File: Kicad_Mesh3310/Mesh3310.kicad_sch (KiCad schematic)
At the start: 12 parts, among them J1 USB device, SW2 "OK"

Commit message: Adding testpoints
Test pint on usb and SWD debug
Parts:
- added TP10: GND, TestPoint:TestPoint_Pad_D1.5mm, symbol Connector:TestPoint
- added TP11: USB_D-, TestPoint:TestPoint_Pad_D1.5mm, symbol Connector:TestPoint
- added TP12: USB_D+, TestPoint:TestPoint_Pad_D1.5mm, symbol Connector:TestPoint
- added TP9: VBUS, TestPoint:TestPoint_Pad_D1.5mm, symbol Connector:TestPoint
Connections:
- net GND: now also TP10.1
- net VBUS: now also TP9.1

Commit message: component placing
component placing
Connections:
- net USB_D+: now also TP12.1
- net USB_D-: now also TP11.1
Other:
- moved on the sheet: TP11, TP12
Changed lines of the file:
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@@
 	)
 	(junction
+		(at 237.49 96.52)
+		(diameter 0)
+		(color 0 0 0 0)
+	)
+	(junction
 		(at 234.95 82.55)
 		(diameter 0)
@@
 	)
 	(junction
+		(at 234.95 91.44)
+		(diameter 0)
+		(color 0 0 0 0)
+	)
+	(junction
 		(at 243.84 91.44)
 		(diameter 0)
@@
 	(wire
 		(pts
+			(xy 237.49 99.06) (xy 237.49 96.52)
+		)
+		(stroke
+			(width 0)
+			(type default)
+		)
+	)
+	(wire
+		(pts
 			(xy 110.49 45.72) (xy 135.89 45.72)
 		)
@@
 	(wire
 		(pts
-			(xy 243.84 96.52) (xy 232.41 96.52)
+			(xy 243.84 96.52) (xy 237.49 96.52)
 		)
 		(stroke
@@
 	(wire
 		(pts
-			(xy 243.84 91.44) (xy 232.41 91.44)
+			(xy 243.84 91.44) (xy 234.95 91.44)
 		)
 		(stroke
@@
 	(wire
 		(pts
+			(xy 234.95 99.06) (xy 234.95 91.44)
+		)
+		(stroke
+			(width 0)
+			(type default)
+		)
+	)
+	(wire
+		(pts
 			(xy 82.55 93.98) (xy 62.23 93.98)
 		)
@@
 		)
 	)
+	(wire
+		(pts
+			(xy 237.49 96.52) (xy 232.41 96.52)
+		)
+		(stroke
+			(width 0)
+			(type default)
+		)
+	)
+	(wire
+		(pts
+			(xy 234.95 91.44) (xy 232.41 91.44)
+		)
+		(stroke
+			(width 0)
+			(type default)
+		)
+	)
 	(bus
 		(pts
@@
 	(symbol
 		(lib_id "Connector:TestPoint")
-		(at 229.87 88.9 90)
+		(at 234.95 99.06 180)
 		(unit 1)
 		(exclude_from_sim no)
@@
 		(dnp no)
 		(property "Reference" "TP11"
-			(at 227.33 87.122 90)
+			(at 233.172 101.6 90)
 			(effects
 				(font
@@
 		)
 		(property "Value" "USB_D-"
-			(at 225.806 85.09 90)
+			(at 231.14 101.6 90)
 			(effects
 				(font
@@
 		)
 		(property "Footprint" "TestPoint:TestPoint_Pad_D1.5mm"
-			(at 229.87 83.82 0)
+			(at 229.87 99.06 0)
 			(effects
 				(font
@@
 		)
 		(property "Datasheet" "~"
-			(at 229.87 83.82 0)
+			(at 229.87 99.06 0)
 			(effects
 				(font
@@
 		)
 		(property "Description" "test point"
-			(at 229.87 88.9 0)
+			(at 234.95 99.06 0)
 			(effects
 				(font
@@
 	(symbol
 		(lib_id "Connector:TestPoint")
-		(at 229.87 93.98 90)
+		(at 237.49 99.06 180)
 		(unit 1)
 		(exclude_from_sim no)
@@
 		(dnp no)
 		(property "Reference" "TP12"
-			(at 228.092 95.758 90)
+			(at 239.268 100.838 90)
 			(effects
 				(font
@@
 		)
 		(property "Value" "USB_D+"
-			(at 227.076 97.536 90)
+			(at 241.046 101.854 90)
 			(effects
 				(font
@@
 		)
 		(property "Footprint" "TestPoint:TestPoint_Pad_D1.5mm"
-			(at 229.87 88.9 0)
+			(at 232.41 99.06 0)
 			(effects
 				(font
@@
 		)
 		(property "Datasheet" "~"
-			(at 229.87 88.9 0)
+			(at 232.41 99.06 0)
 			(effects
 				(font
@@
 		)
 		(property "Description" "test point"
-			(at 229.87 93.98 0)
+			(at 237.49 99.06 0)
 			(effects
 				(font

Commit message: Cleaning and placing
Cleaning and placing components
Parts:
- H1, H2, H3, H4, H5, H6, H7: footprint Parts:2mm_mounting_hole_sig -> mesh3310_footprints:2mm_mounting_hole_sig
- J1: footprint mesh3310:USB_C_Receptacle_HRO_TYPE-C-31-M-12 -> mesh3310_footprints:USB_C_Receptacle_HRO_TYPE-C-31-M-12
- SW2: footprint Parts:3310_key -> mesh3310_footprints:3310_key
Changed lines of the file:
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@@
 			)
 		)
-		(property "Footprint" "Parts:2mm_mounting_hole_sig"
+		(property "Footprint" "mesh3310_footprints:2mm_mounting_hole_sig"
 			(at 107.95 175.26 0)
 			(effects
@@
 			)
 		)
-		(property "Footprint" "Parts:2mm_mounting_hole_sig"
+		(property "Footprint" "mesh3310_footprints:2mm_mounting_hole_sig"
 			(at 100.33 175.26 0)
 			(effects
@@
 			)
 		)
-		(property "Footprint" "Parts:2mm_mounting_hole_sig"
+		(property "Footprint" "mesh3310_footprints:2mm_mounting_hole_sig"
 			(at 146.05 175.26 0)
 			(effects
@@
 			)
 		)
-		(property "Footprint" "Parts:2mm_mounting_hole_sig"
+		(property "Footprint" "mesh3310_footprints:2mm_mounting_hole_sig"
 			(at 115.57 175.26 0)
 			(effects
@@
 			)
 		)
-		(property "Footprint" "Parts:2mm_mounting_hole_sig"
+		(property "Footprint" "mesh3310_footprints:2mm_mounting_hole_sig"
 			(at 130.81 175.26 0)
 			(effects
@@
 			)
 		)
-		(property "Footprint" "Parts:2mm_mounting_hole_sig"
+		(property "Footprint" "mesh3310_footprints:2mm_mounting_hole_sig"
 			(at 138.43 175.26 0)
 			(effects
@@
 			)
 		)
-		(property "Footprint" "Parts:2mm_mounting_hole_sig"
+		(property "Footprint" "mesh3310_footprints:2mm_mounting_hole_sig"
 			(at 123.19 175.26 0)
 			(effects
@@
 			)
 		)
-		(property "Footprint" "mesh3310:USB_C_Receptacle_HRO_TYPE-C-31-M-12"
+		(property "Footprint" "mesh3310_footprints:USB_C_Receptacle_HRO_TYPE-C-31-M-12"
 			(at 256.54 92.71 0)
 			(effects
@@
 			)
 		)
-		(property "Footprint" "Parts:3310_key"
+		(property "Footprint" "mesh3310_footprints:3310_key"
 			(at 109.22 33.02 0)
 			(effects

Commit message: RF designing
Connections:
- no-connect marks 9 -> 11
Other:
- removed sheet NFC
- note added: "Used with permission / community credit Reference designs and libs from badge.team MCU sections adapted from CyberAegg."
- note removed: "Used with permission / community credit Reference designs and libs from badge.team MCU and RF sections adapted from CyberAegg."
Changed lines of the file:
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@@
 		)
 	)
-	(text "Used with permission / community credit\nReference designs and libs from badge.team\nMCU and RF sections adapted from CyberAegg.\n\n"
+	(text "Used with permission / community credit\nReference designs and libs from badge.team\nMCU sections adapted from CyberAegg.\n\n"
 		(exclude_from_sim no)
 		(at 240.03 176.53 0)
@@
 	)
 	(no_connect
+		(at 135.89 43.18)
+	)
+	(no_connect
 		(at 179.07 29.21)
 	)
@@
 	)
 	(no_connect
+		(at 135.89 45.72)
+	)
+	(no_connect
 		(at 245.11 105.41)
 	)
@@
 	(wire
 		(pts
-			(xy 110.49 43.18) (xy 135.89 43.18)
-		)
-		(stroke
-			(width 0)
-			(type default)
-		)
-	)
-	(wire
-		(pts
 			(xy 195.58 130.81) (xy 175.26 130.81)
 		)
@@
 	(wire
 		(pts
-			(xy 110.49 45.72) (xy 135.89 45.72)
-		)
-		(stroke
-			(width 0)
-			(type default)
-		)
-	)
-	(wire
-		(pts
 			(xy 200.66 31.75) (xy 179.07 31.75)
 		)
@@
 	)
 	(sheet
-		(at 82.55 41.91)
-		(size 27.94 5.08)
-		(exclude_from_sim no)
-		(in_bom yes)
-		(on_board yes)
-		(dnp no)
-		(stroke
-			(width 0.1524)
-			(type solid)
-		)
-		(fill
-			(color 0 0 0 0.0000)
-		)
-		(property "Sheetname" "NFC"
-			(at 82.296 41.148 0)
-			(effects
-				(font
-					(size 1.27 1.27)
-				)
-				(justify left bottom)
-			)
-		)
-		(property "Sheetfile" "nfc.kicad_sch"
-			(at 82.55 47.5746 0)
-			(effects
-				(font
-					(size 1.27 1.27)
-				)
-				(justify left top)
-			)
-		)
-		(pin "NFC1" input
-			(at 110.49 43.18 0)
-			(effects
-				(font
-					(size 1.27 1.27)
-				)
-				(justify right)
-			)
-		)
-		(pin "NFC2" input
-			(at 110.49 45.72 0)
-			(effects
-				(font
-					(size 1.27 1.27)
-				)
-				(justify right)
-			)
-		)
-		(instances
-			(project "Mesh3310"
-				(path "/8d65c5ef-7a02-4454-aee5-ab9c49e4aeab"
-					(page "5")
-				)
-			)
-		)
-	)
-	(sheet
 		(at 41.91 67.31)
 		(size 20.32 40.64)
@@
 			(project "Mesh3310"
 				(path "/8d65c5ef-7a02-4454-aee5-ab9c49e4aeab"
-					(page "7")
+					(page "6")
 				)
 			)
@@
 			(project "Mesh3310"
 				(path "/8d65c5ef-7a02-4454-aee5-ab9c49e4aeab"
-					(page "6")
+					(page "5")
 				)
 			)

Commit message: cleanup
schematic cleanup
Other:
- removed sheet QWIIC
- sheet INTERFACES ports: added SCL, SDA; removed none
- note added: "JLC04161H-7628 Stackup Impendance calculator: https://jlcpcb.com/pcb-impedance-calculator"
- note added: "Used with permission / community credit Reference designs MCU sections adapted from CyberAegg. badge.team"
- note removed: "JLCPCB Inpedance control Stackup used: JLC04161H-7628 Stackup Impendance calculator: https://jlcpcb.com/pcb-impedance-calculator"
- note removed: "Used with permission / community credit Reference designs and libs from badge.team MCU sections adapted from CyberAegg."
- moved on the sheet: H1, H2, H3, H4, H5, H6, H7, J1, R1, R2, R8, SW2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

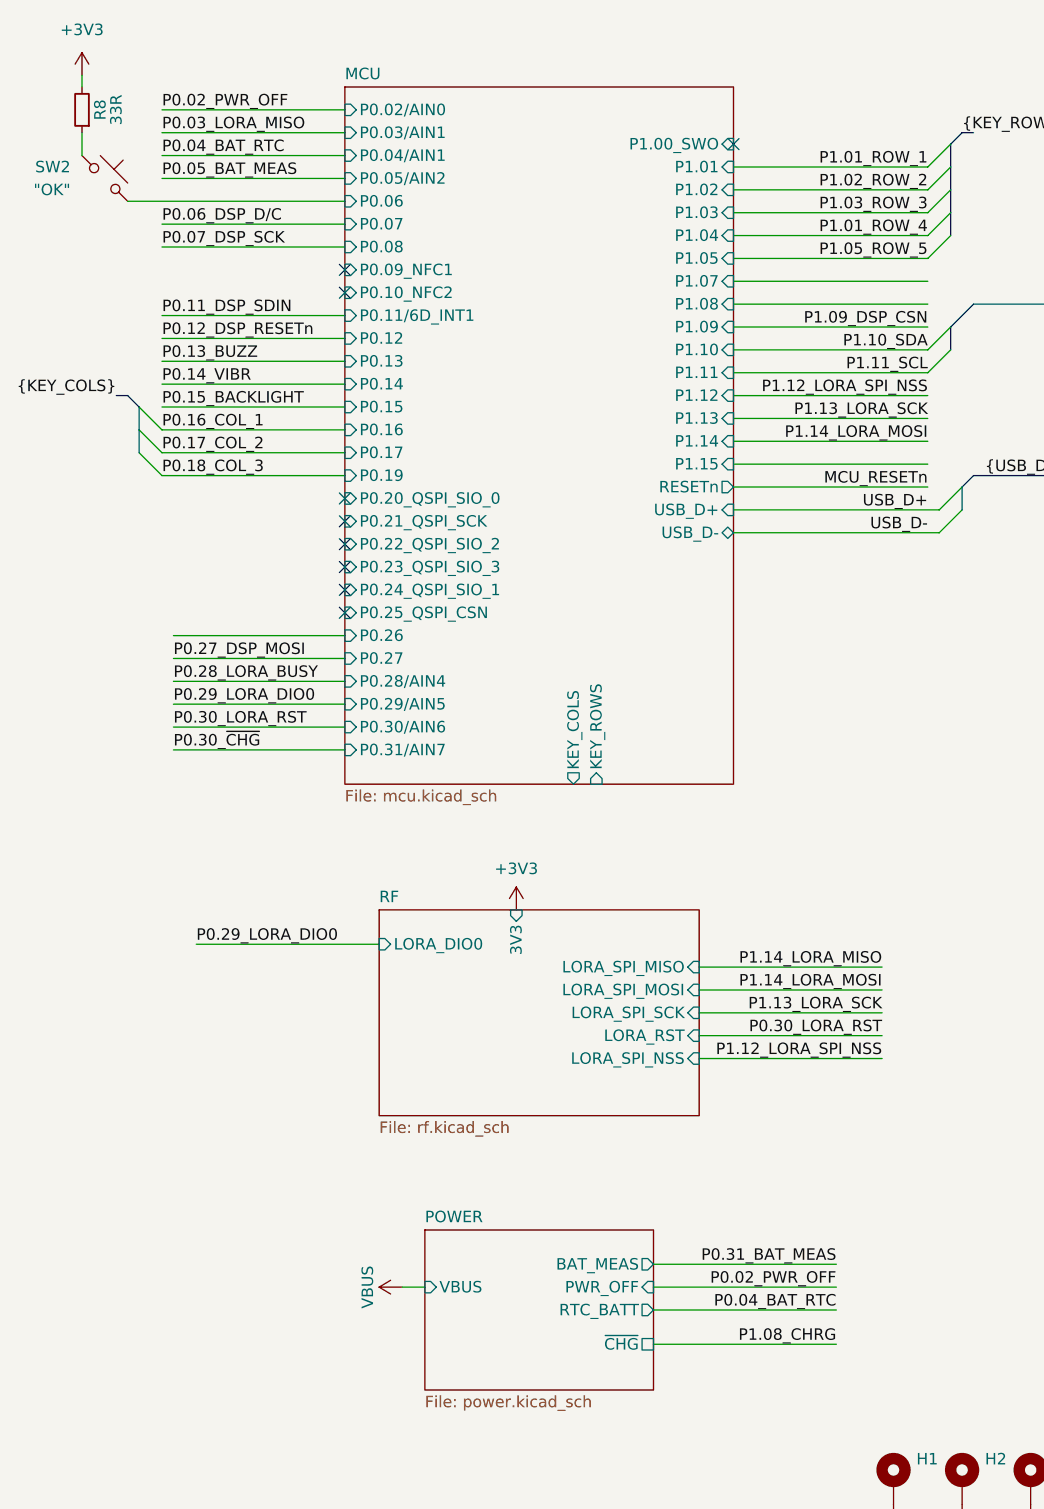
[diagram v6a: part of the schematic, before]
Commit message: Lora changes
Schematic changes to from RA to SOC
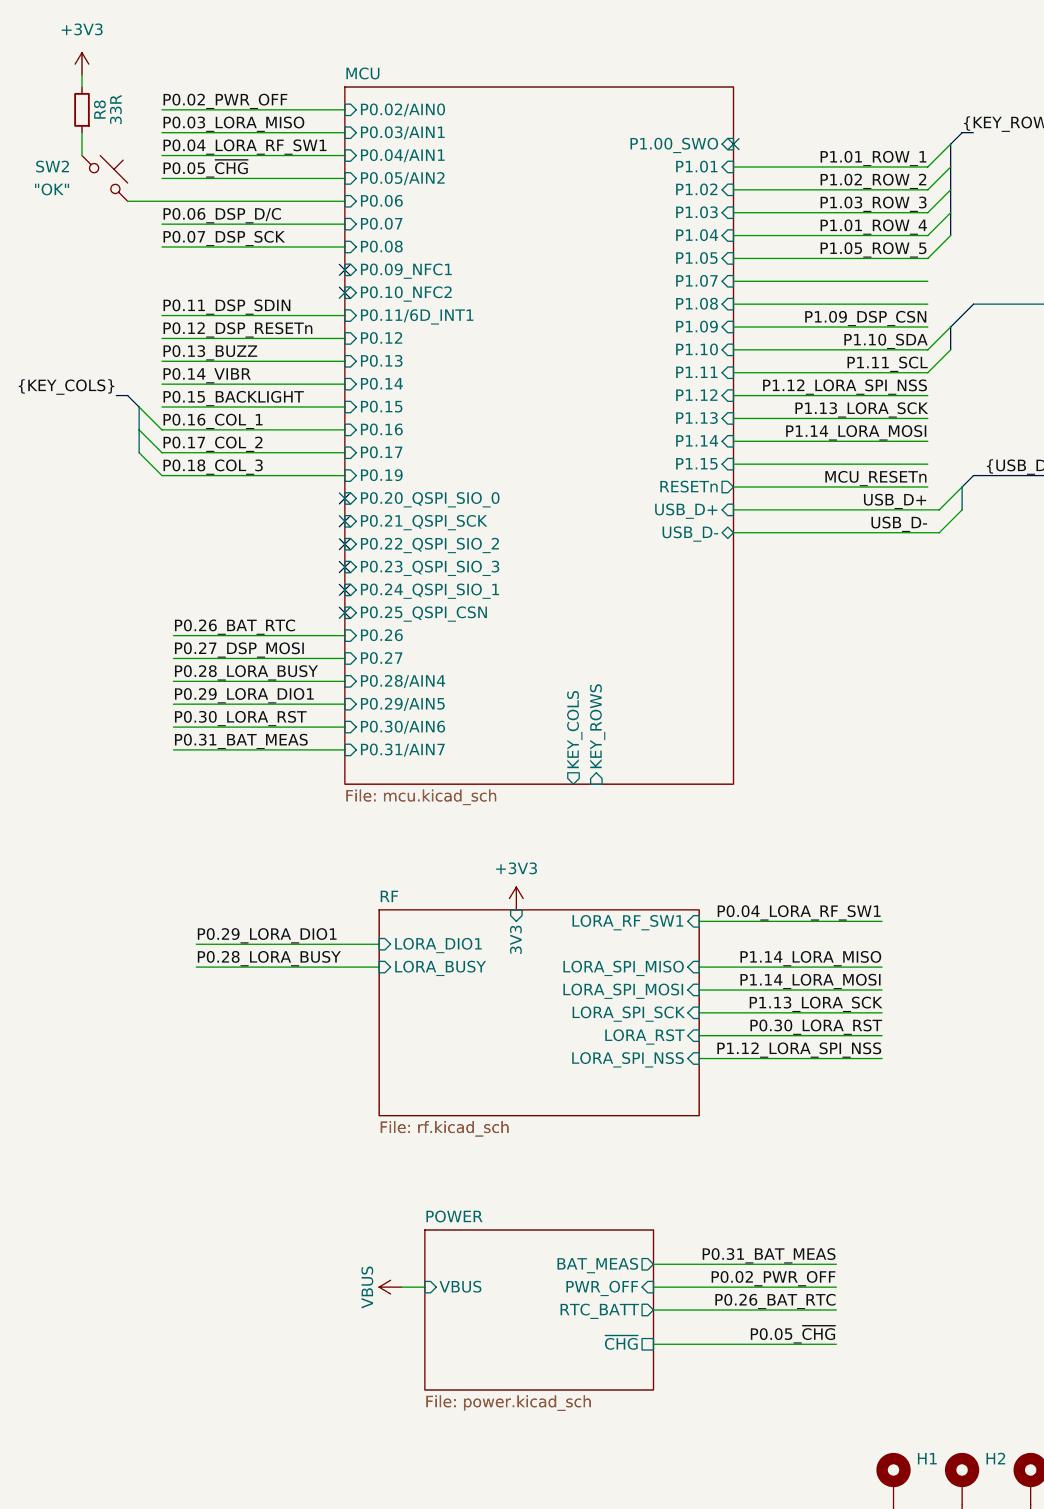
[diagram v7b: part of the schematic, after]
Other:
- sheet RF ports: added LORA_BUSY, LORA_DIO1, LORA_RF_SW1; removed LORA_DIO0
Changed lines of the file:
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@@
 		)
 	)
+	(wire
+		(pts
+			(xy 64.77 130.81) (xy 44.45 130.81)
+		)
+		(stroke
+			(width 0)
+			(type default)
+		)
+	)
 	(bus
 		(pts
@@
 	(wire
 		(pts
+			(xy 100.33 125.73) (xy 120.65 125.73)
+		)
+		(stroke
+			(width 0)
+			(type default)
+		)
+	)
+	(wire
+		(pts
 			(xy 100.33 140.97) (xy 120.65 140.97)
 		)
@@
 		)
 	)
-	(label "P1.08_CHRG"
+	(label "P0.05_~{CHG}"
 		(at 115.57 172.72 180)
 		(effects
@@
 		)
 	)
-	(label "P0.29_LORA_DIO0"
+	(label "P0.29_LORA_DIO1"
 		(at 44.45 128.27 0)
 		(effects
@@
 		)
 	)
+	(label "P0.04_LORA_RF_SW1"
+		(at 120.65 125.73 180)
+		(effects
+			(font
+				(size 1.27 1.27)
+			)
+			(justify right bottom)
+		)
+	)
 	(label "CC2"
 		(at 170.18 95.25 180)
@@
 		)
 	)
-	(label "P0.30_~{CHG}"
-		(at 41.91 106.68 0)
+	(label "P0.05_~{CHG}"
+		(at 40.64 43.18 0)
 		(effects
 			(font
@@
 		)
 	)
-	(label "P0.04_BAT_RTC"
-		(at 40.64 40.64 0)
+	(label "P0.26_BAT_RTC"
+		(at 41.91 93.98 0)
 		(effects
 			(font
@@
 		)
 	)
-	(label "P0.29_LORA_DIO0"
+	(label "P0.29_LORA_DIO1"
 		(at 41.91 101.6 0)
 		(effects
@@
 		)
 	)
+	(label "P0.04_LORA_RF_SW1"
+		(at 40.64 40.64 0)
+		(effects
+			(font
+				(size 1.27 1.27)
+			)
+			(justify left bottom)
+		)
+	)
 	(label "P1.14_LORA_MOSI"
 		(at 120.65 133.35 180)
@@
 		)
 	)
-	(label "P0.04_BAT_RTC"
+	(label "P0.26_BAT_RTC"
 		(at 115.57 168.91 180)
 		(effects
@@
 		)
 	)
+	(label "P0.28_LORA_BUSY"
+		(at 44.45 130.81 0)
+		(effects
+			(font
+				(size 1.27 1.27)
+			)
+			(justify left bottom)
+		)
+	)
 	(label "P1.12_LORA_SPI_NSS"
 		(at 120.65 140.97 180)
@@
 		)
 	)
-	(label "P0.05_BAT_MEAS"
-		(at 40.64 43.18 0)
+	(label "P0.31_BAT_MEAS"
+		(at 41.91 106.68 0)
 		(effects
 			(font
@@
 			)
 		)
-		(pin "LORA_DIO0" input
+		(pin "LORA_BUSY" input
+			(at 64.77 130.81 180)
+			(effects
+				(font
+					(size 1.27 1.27)
+				)
+				(justify left)
+			)
+		)
+		(pin "LORA_DIO1" input
 			(at 64.77 128.27 180)
 			(effects
@@
 			)
 		)
+		(pin "LORA_RF_SW1" input
+			(at 100.33 125.73 0)
+			(effects
+				(font
+					(size 1.27 1.27)
+				)
+				(justify right)
+			)
+		)

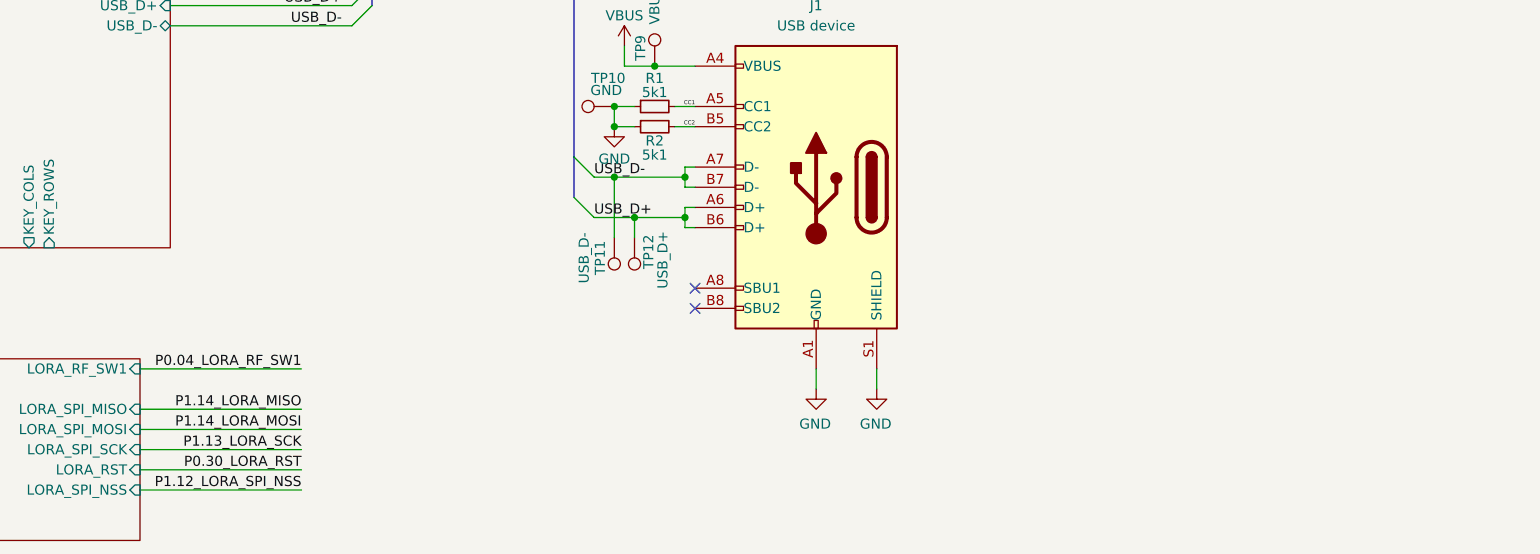
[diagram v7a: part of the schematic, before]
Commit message: Lora antenna replacement
Lora antenna replacement, added Nordic nRF 9151 for GPS , VoIP ,VoLTE-m , SIP
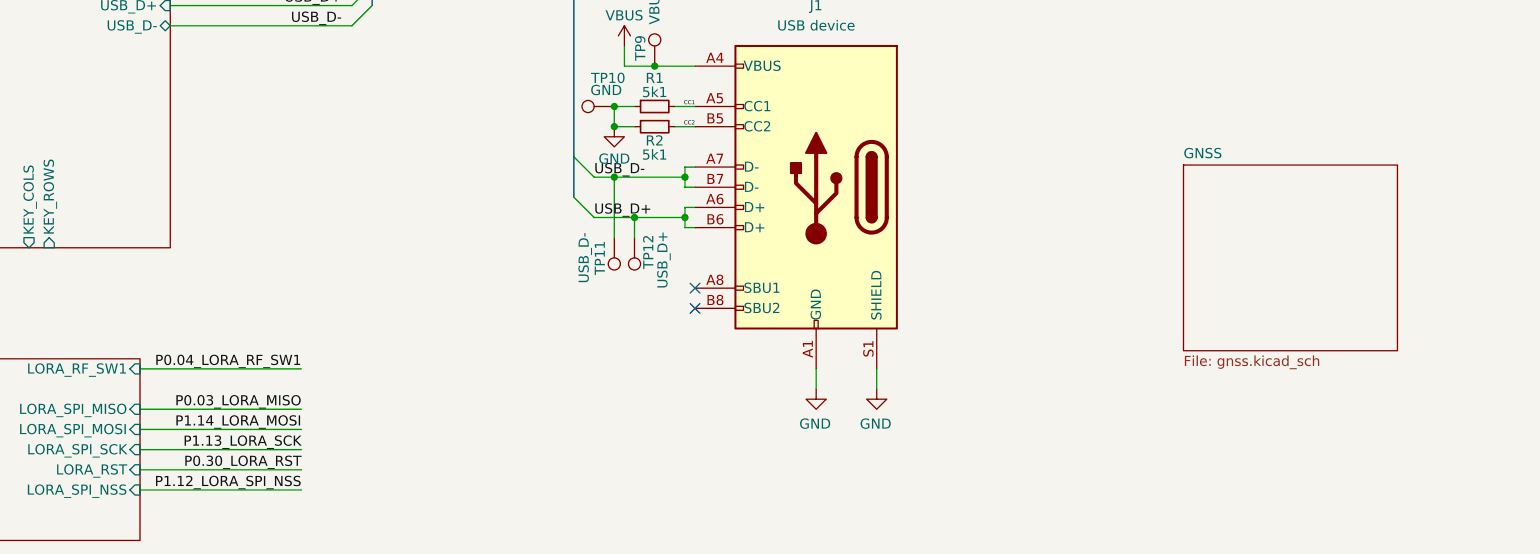
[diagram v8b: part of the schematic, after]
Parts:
- R1, R2, R8: footprint Resistor_SMD:R_0402_1005Metric -> Resistor_SMD:R_0201_0603Metric
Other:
- added sheet GNSS (gnss.kicad_sch)
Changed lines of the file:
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@@
 		)
 	)
-	(label "P1.14_LORA_MISO"
+	(label "P0.03_LORA_MISO"
 		(at 120.65 130.81 180)
 		(effects
@@
 			)
 		)
-		(property "Footprint" "Resistor_SMD:R_0402_1005Metric"
+		(property "Footprint" "Resistor_SMD:R_0201_0603Metric"
 			(at 165.1 92.71 0)
 			(effects
@@
 			)
 		)
-		(property "Footprint" "Resistor_SMD:R_0402_1005Metric"
+		(property "Footprint" "Resistor_SMD:R_0201_0603Metric"
 			(at 31.75 35.56 0)
 			(effects
@@
 			)
 		)
-		(property "Footprint" "Resistor_SMD:R_0402_1005Metric"
+		(property "Footprint" "Resistor_SMD:R_0201_0603Metric"
 			(at 165.1 95.25 0)
 			(effects
@@
 				)
 			)
+		)
+	)
+	(sheet
+		(at 231.648 100.076)
+		(size 26.924 23.368)
+		(exclude_from_sim no)
+		(in_bom yes)
+		(on_board yes)
+		(dnp no)
+		(fields_autoplaced yes)
+		(stroke
+			(width 0.1524)
+			(type solid)
+		)
+		(fill
+			(color 0 0 0 0.0000)
+		)
+		(property "Sheetname" "GNSS"
+			(at 231.648 99.3644 0)
+			(effects
+				(font
+					(size 1.27 1.27)
+				)
+				(justify left bottom)
+			)
+		)
+		(property "Sheetfile" "gnss.kicad_sch"
+			(at 231.648 124.0286 0)
+			(effects
+				(font
+					(size 1.27 1.27)
+				)
+				(justify left top)
+			)
+		)
+		(instances
+			(project "Mesh3310"
+				(path "/8d65c5ef-7a02-4454-aee5-ab9c49e4aeab"
+					(page "6")
+				)
+			)
